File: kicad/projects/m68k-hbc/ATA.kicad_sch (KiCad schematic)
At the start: 4 parts, among them U18 74LS245, U19 74LS245

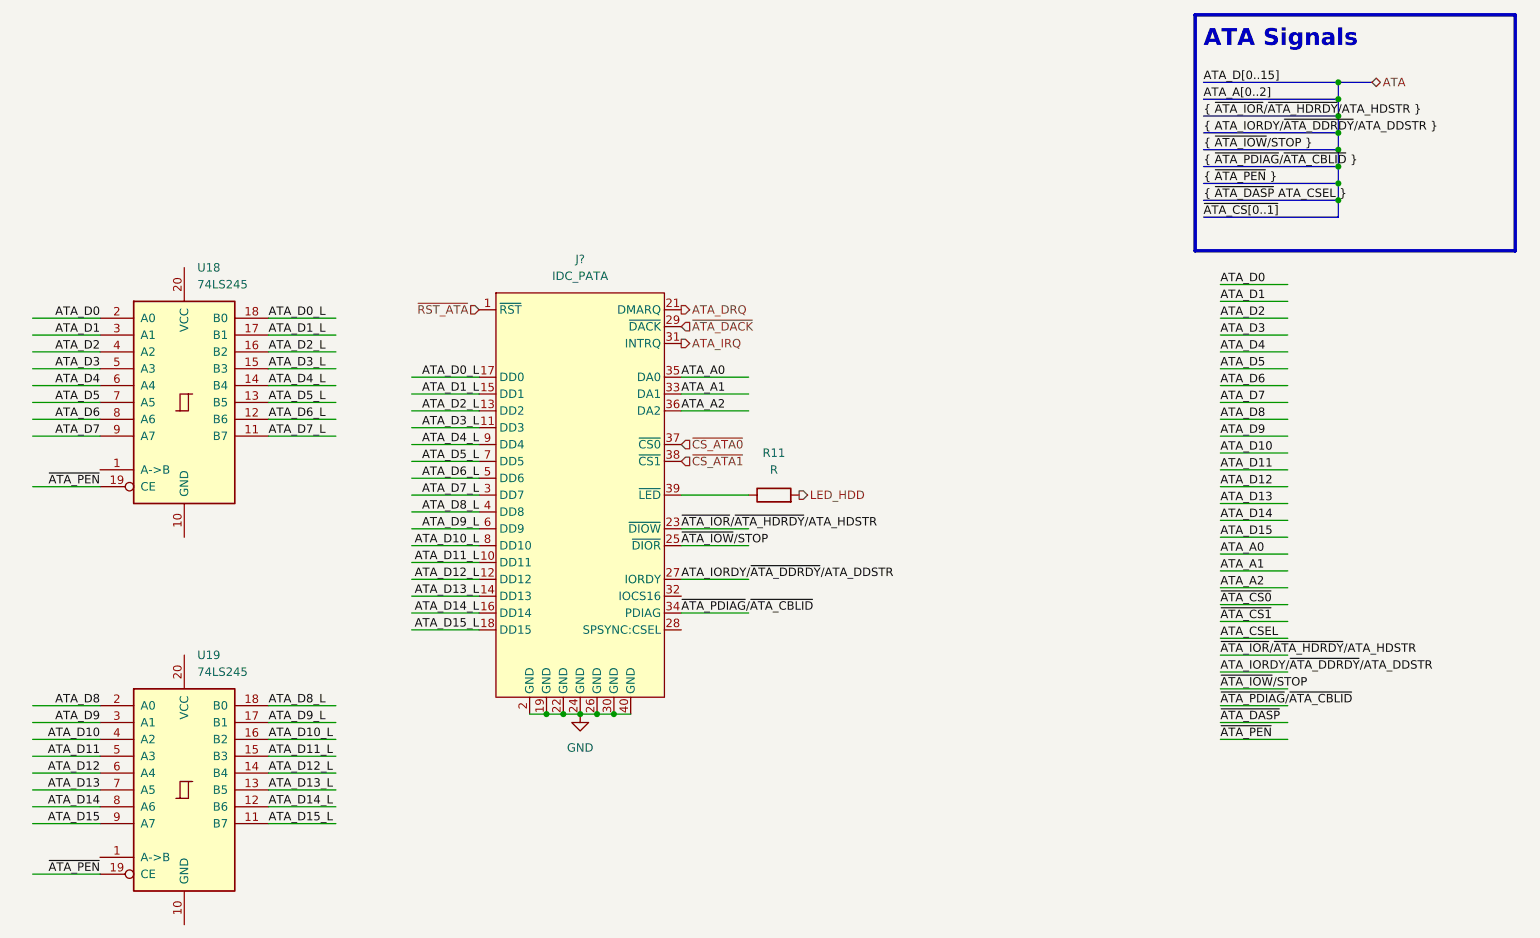
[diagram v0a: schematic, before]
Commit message: Large changes: EHBCSimpleEmu, kicad, fwcode, docs
This commit contains some large changes:
- Removed EHBCSimpleEmu (Moved to kms1212/llemu, kms1212/qemu)
- (likely) Removed fwcode; now it only boots and stops
- Modified documents
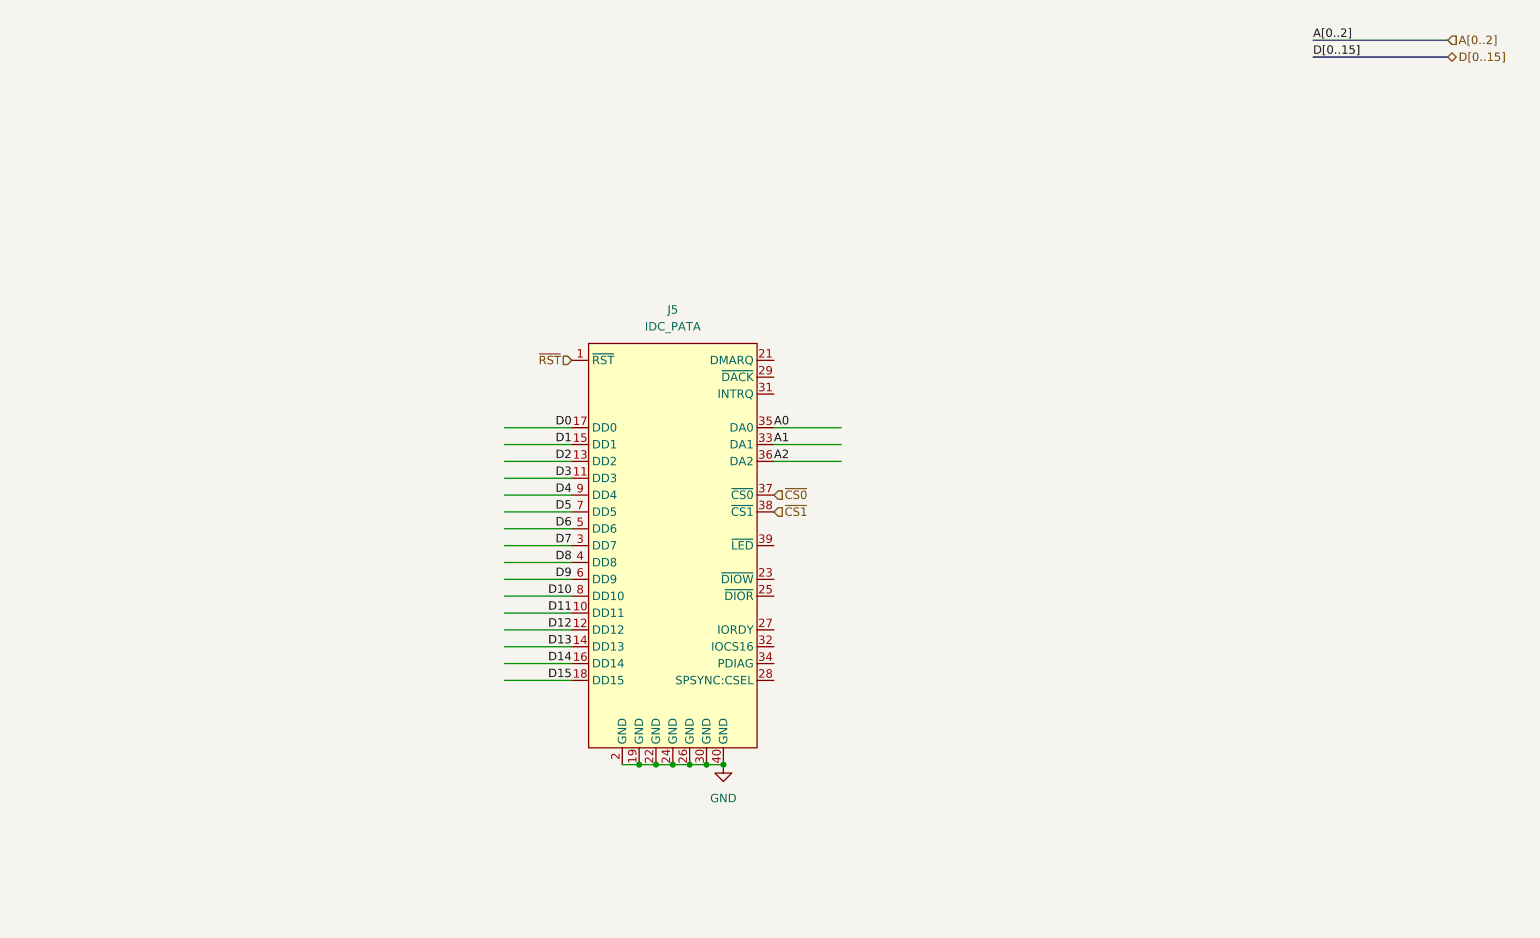
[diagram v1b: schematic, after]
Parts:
- removed J?: IDC_PATA, Connector_IDC:IDC-Header_2x20_P2.54mm_Vertical, symbol IDC_SpecialPurpose:IDC_PATA
- removed R11: R, Resistor_SMD:R_0603_1608Metric_Pad0.98x0.95mm_HandSolder, symbol Device:R
- removed U18, U19: 74LS245, symbol 74xx:74LS245
- added J5: IDC_PATA, Connector_IDC:IDC-Header_2x20_P2.54mm_Vertical, symbol m68k-hbc-conn:IDC_PATA
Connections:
- net GND: now also J5.19 (GND), J5.2 (GND), J5.22 (GND), J5.24 (GND), J5.26 (GND), J5.30 (GND), J5.40 (GND)
- new net A0: J5.35 (DA0)
- new net A1: J5.33 (DA1)
- new net A2: J5.36 (DA2)
- new net D0: J5.17 (DD0)
- new net D1: J5.15 (DD1)
- new net D10: J5.8 (DD10)
- new net D11: J5.10 (DD11)
- new net D12: J5.12 (DD12)
- new net D13: J5.14 (DD13)
- new net D14: J5.16 (DD14)
- new net D15: J5.18 (DD15)
- new net D2: J5.13 (DD2)
- new net D3: J5.11 (DD3)
- new net D4: J5.9 (DD4)
- new net D5: J5.7 (DD5)
- new net D6: J5.5 (DD6)
- new net D7: J5.3 (DD7)
- new net D8: J5.4 (DD8)
- new net D9: J5.6 (DD9)
- new net ~{CS0}: J5.37 (~{CS0})
- new net ~{CS1}: J5.38 (~{CS1})
- new net ~{RST}: J5.1 (~{RST})
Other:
- note removed: "ATA Signals"
